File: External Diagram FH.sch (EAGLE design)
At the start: 81 parts

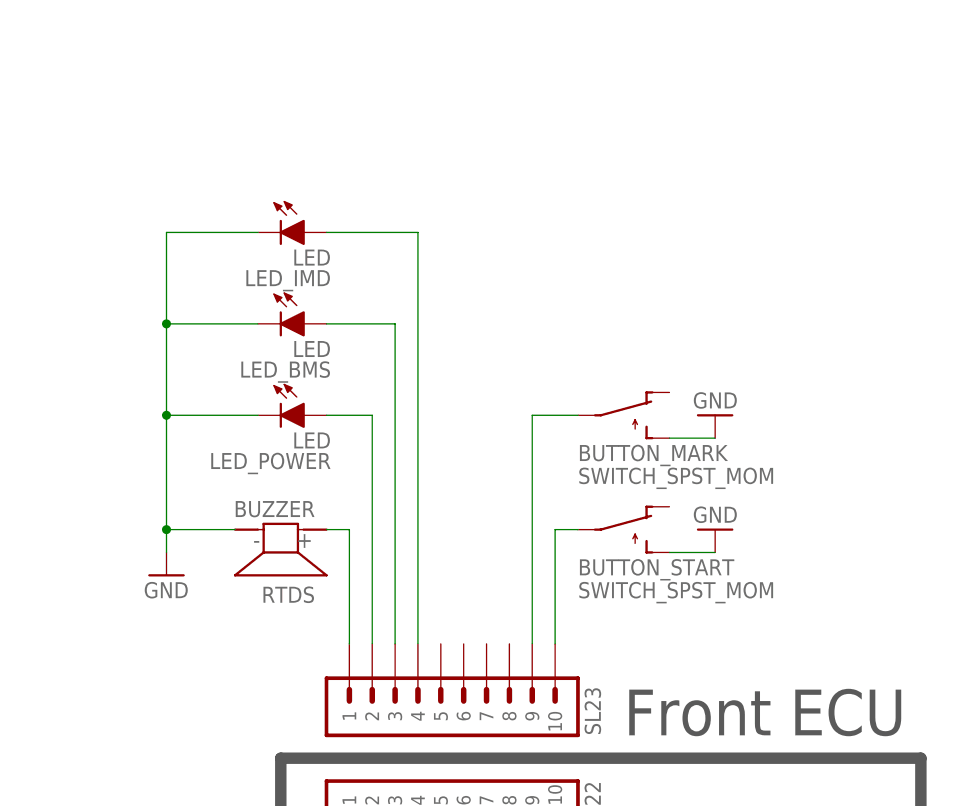
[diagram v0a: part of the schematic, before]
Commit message: Updates to wiring diagrams
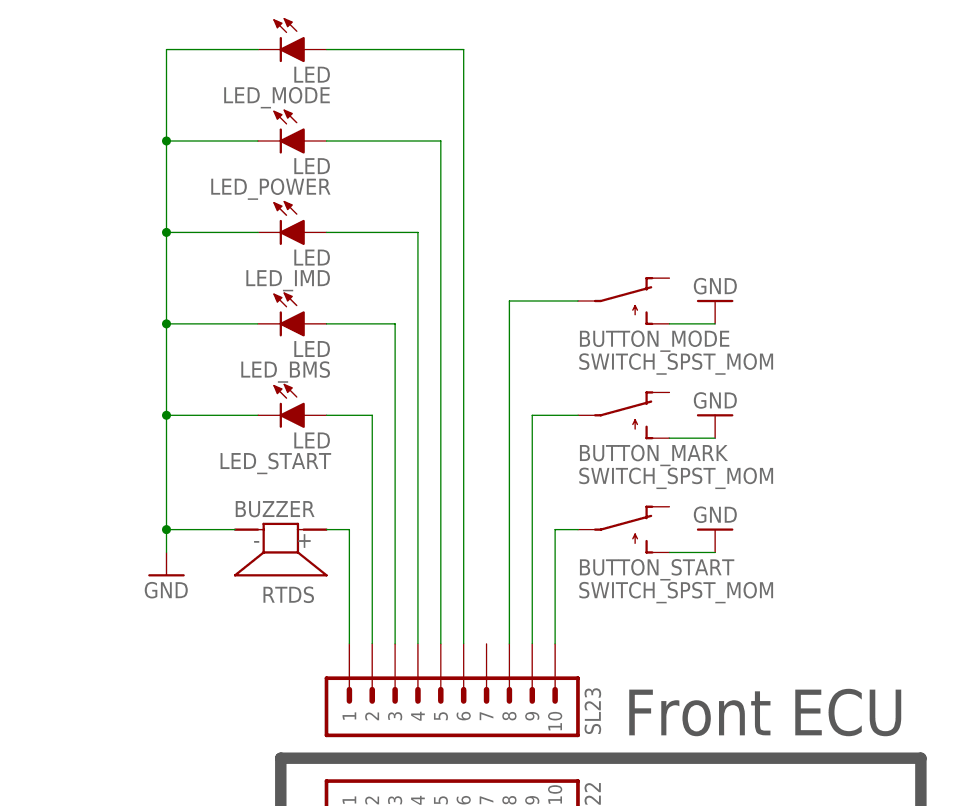
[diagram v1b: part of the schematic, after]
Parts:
- added BUTTON_MODE: SWITCH_SPST_MOM, HyTechSymbols:SWITCH_SPST_MOM
- added LED_MODE, LED_START: LED, HyTechSymbols:LED
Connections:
- new net N$3: LED_POWER.A, SL23.5
- new net N$5: LED_MODE.A, SL23.6
- new net N$6: BUTTON_MODE.P, SL23.8
- net GND: now also BUTTON_MODE.S, LED_MODE.C, LED_START.C
- net N$2: now also LED_START.A; no longer LED_POWER.A
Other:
- moved on the sheet: LED_POWER
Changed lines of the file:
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@@
 <part name="LED_BMS" library="HyTechSymbols" deviceset="LED" device=""/>
 <part name="LED_IMD" library="HyTechSymbols" deviceset="LED" device=""/>
-<part name="LED_POWER" library="HyTechSymbols" deviceset="LED" device=""/>
+<part name="LED_START" library="HyTechSymbols" deviceset="LED" device=""/>
 <part name="SL12" library="HyTechSymbols" deviceset="M04" device=""/>
 <part name="GND2" library="HyTechSymbols" deviceset="GND" device=""/>
@@
 <part name="PRE_F2" library="HyTechSymbols" deviceset="FUSE" device="" value="6.3A"/>
 <part name="PRE_F1" library="HyTechSymbols" deviceset="FUSE" device="" value="6.3A"/>
+<part name="BUTTON_MODE" library="HyTechSymbols" deviceset="SWITCH_SPST_MOM" device=""/>
+<part name="GND20" library="HyTechSymbols" deviceset="GND" device=""/>
+<part name="LED_POWER" library="HyTechSymbols" deviceset="LED" device=""/>
+<part name="LED_MODE" library="HyTechSymbols" deviceset="LED" device=""/>
 </parts>
 <sheets>
@@
 <instance part="LED_BMS" gate="G$1" x="533.4" y="297.18" rot="R180"/>
 <instance part="LED_IMD" gate="G$1" x="533.4" y="307.34" rot="R180"/>
-<instance part="LED_POWER" gate="G$1" x="533.4" y="287.02" rot="R180"/>
+<instance part="LED_START" gate="G$1" x="533.4" y="287.02" rot="R180"/>
 <instance part="SL12" gate="G$1" x="22.86" y="190.5" rot="R180"/>
 <instance part="GND2" gate="1" x="246.38" y="-5.08" rot="R270"/>
@@
 <instance part="PRE_F2" gate="G$1" x="208.28" y="241.3"/>
 <instance part="PRE_F1" gate="G$1" x="203.2" y="259.08"/>
+<instance part="BUTTON_MODE" gate="SPST_MOM" x="566.42" y="297.18" rot="R270"/>
+<instance part="GND20" gate="1" x="576.58" y="297.18" rot="R180"/>
+<instance part="LED_POWER" gate="G$1" x="533.4" y="317.5" rot="R180"/>
+<instance part="LED_MODE" gate="G$1" x="533.4" y="327.66" rot="R180"/>
 </instances>
 <busses>
@@
 <pinref part="RTDS" gate="1" pin="2"/>
 <wire x1="523.24" y1="271.78" x2="515.62" y2="271.78" width="0.1524" layer="91"/>
-<pinref part="LED_POWER" gate="G$1" pin="C"/>
+<pinref part="LED_START" gate="G$1" pin="C"/>
 <wire x1="525.78" y1="284.48" x2="515.62" y2="284.48" width="0.1524" layer="91"/>
 <wire x1="515.62" y1="271.78" x2="515.62" y2="284.48" width="0.1524" layer="91"/>
@@
 <wire x1="515.62" y1="304.8" x2="515.62" y2="294.64" width="0.1524" layer="91"/>
 <junction x="515.62" y="294.64"/>
+<pinref part="LED_POWER" gate="G$1" pin="C"/>
+<wire x1="525.78" y1="314.96" x2="515.62" y2="314.96" width="0.1524" layer="91"/>
+<wire x1="515.62" y1="314.96" x2="515.62" y2="304.8" width="0.1524" layer="91"/>
+<junction x="515.62" y="304.8"/>
+<pinref part="LED_MODE" gate="G$1" pin="C"/>
+<wire x1="525.78" y1="325.12" x2="515.62" y2="325.12" width="0.1524" layer="91"/>
+<wire x1="515.62" y1="325.12" x2="515.62" y2="314.96" width="0.1524" layer="91"/>
+<junction x="515.62" y="314.96"/>
 </segment>
 <segment>
@@
 <pinref part="GND18" gate="1" pin="GND"/>
 <wire x1="304.8" y1="66.04" x2="322.58" y2="66.04" width="0.1524" layer="91"/>
+</segment>
+<segment>
+<pinref part="GND20" gate="1" pin="GND"/>
+<pinref part="BUTTON_MODE" gate="SPST_MOM" pin="S"/>
+<wire x1="576.58" y1="294.64" x2="571.5" y2="294.64" width="0.1524" layer="91"/>
 </segment>
 </net>
@@
 <net name="N$2" class="0">
 <segment>
-<pinref part="LED_POWER" gate="G$1" pin="A"/>
+<pinref part="LED_START" gate="G$1" pin="A"/>
 <wire x1="538.48" y1="284.48" x2="533.4" y2="284.48" width="0.1524" layer="91"/>
 <pinref part="SL23" gate="G$1" pin="2"/>
@@
 </segment>
 </net>
+<net name="N$3" class="0">
+<segment>
+<pinref part="SL23" gate="G$1" pin="5"/>
+<wire x1="546.1" y1="259.08" x2="546.1" y2="314.96" width="0.1524" layer="91"/>
+<wire x1="546.1" y1="314.96" x2="533.4" y2="314.96" width="0.1524" layer="91"/>
+<pinref part="LED_POWER" gate="G$1" pin="A"/>
+</segment>
+</net>
+<net name="N$5" class="0">
+<segment>
+<pinref part="SL23" gate="G$1" pin="6"/>
+<wire x1="548.64" y1="259.08" x2="548.64" y2="325.12" width="0.1524" layer="91"/>
+<wire x1="548.64" y1="325.12" x2="533.4" y2="325.12" width="0.1524" layer="91"/>
+<pinref part="LED_MODE" gate="G$1" pin="A"/>
+</segment>
+</net>
+<net name="N$6" class="0">
+<segment>
+<pinref part="SL23" gate="G$1" pin="8"/>
+<wire x1="553.72" y1="259.08" x2="553.72" y2="297.18" width="0.1524" layer="91"/>
+<wire x1="553.72" y1="297.18" x2="561.34" y2="297.18" width="0.1524" layer="91"/>
+<pinref part="BUTTON_MODE" gate="SPST_MOM" pin="P"/>
+</segment>
+</net>
